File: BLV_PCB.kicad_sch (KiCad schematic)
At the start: 8 parts, among them J1 Cube0 JST-PH, J2 Cube0 JST-PH, J3 Cube0 JST-PH, J4 Micro_SD_Card

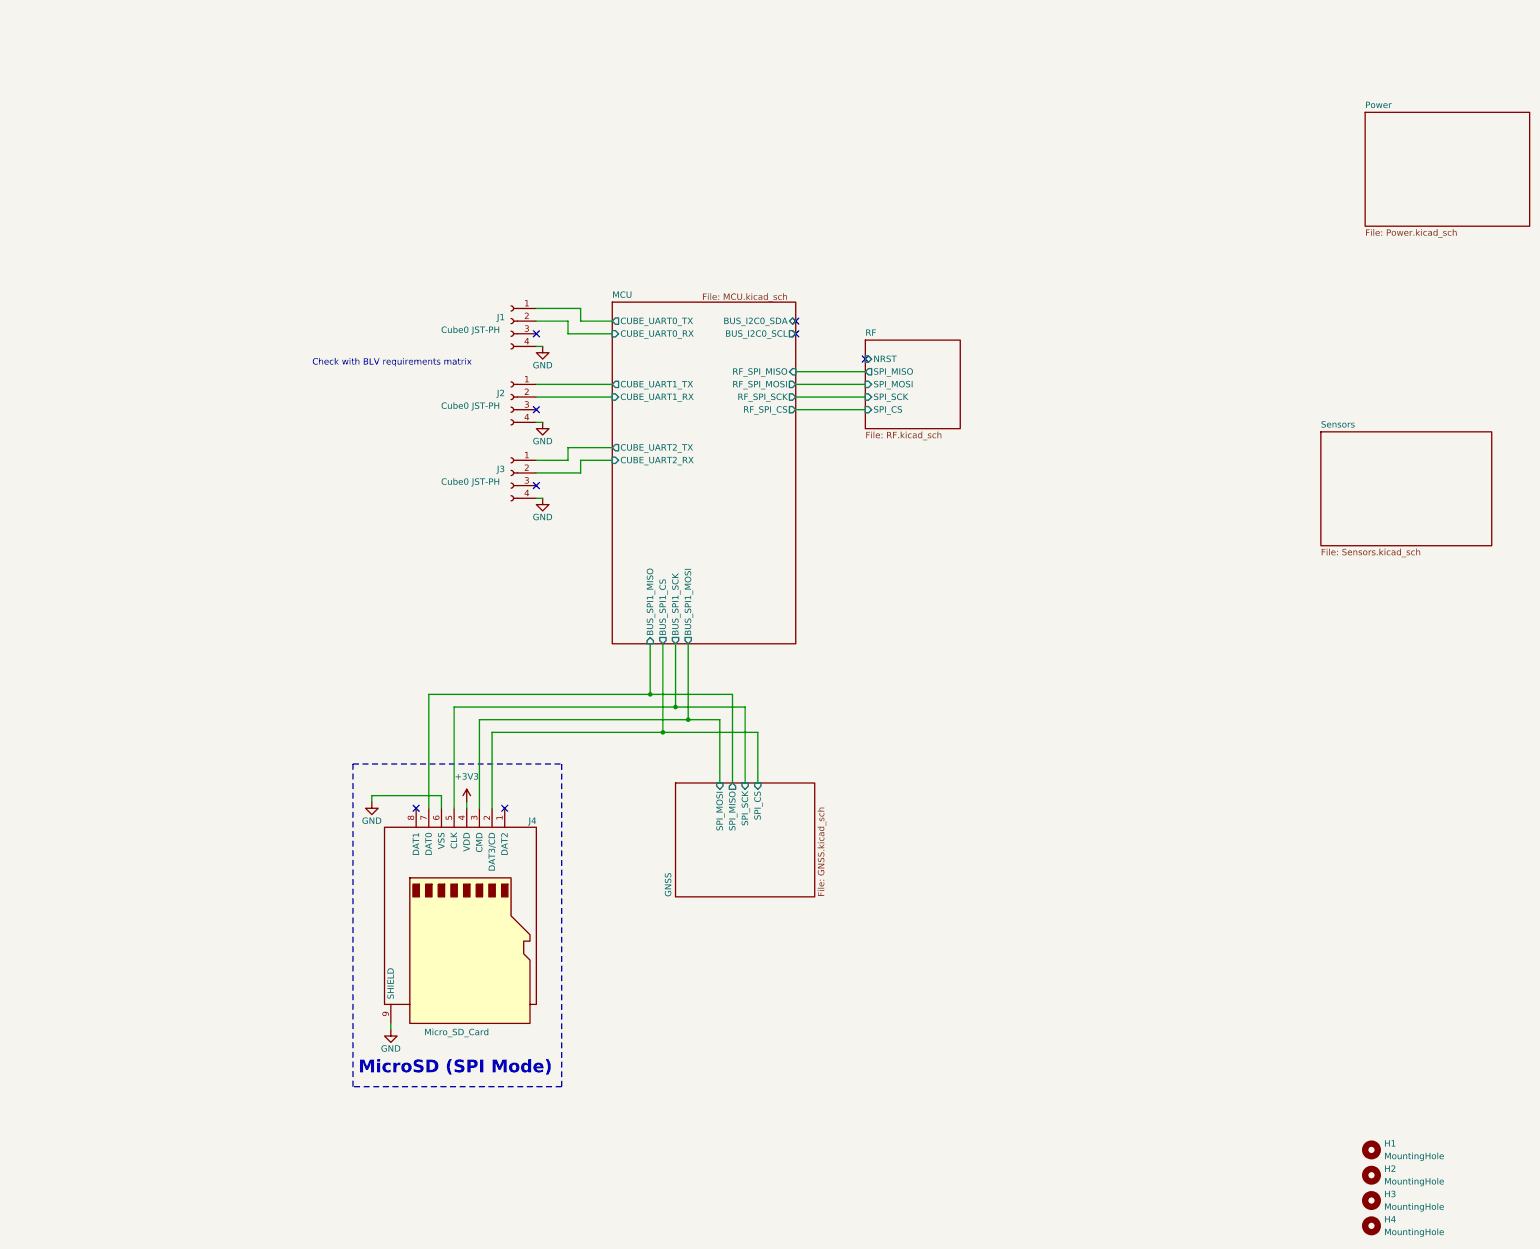
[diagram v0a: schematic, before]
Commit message: Added footprints & routing 30%
- Added Dupont debug headers for UARTs.
- Added footprints: 18650 battery, E32-400M30S.
- Remove Battery Charger due to reliability issue.
- Routing 5V SMPS, 3V3 Regulator, Battery Holder.
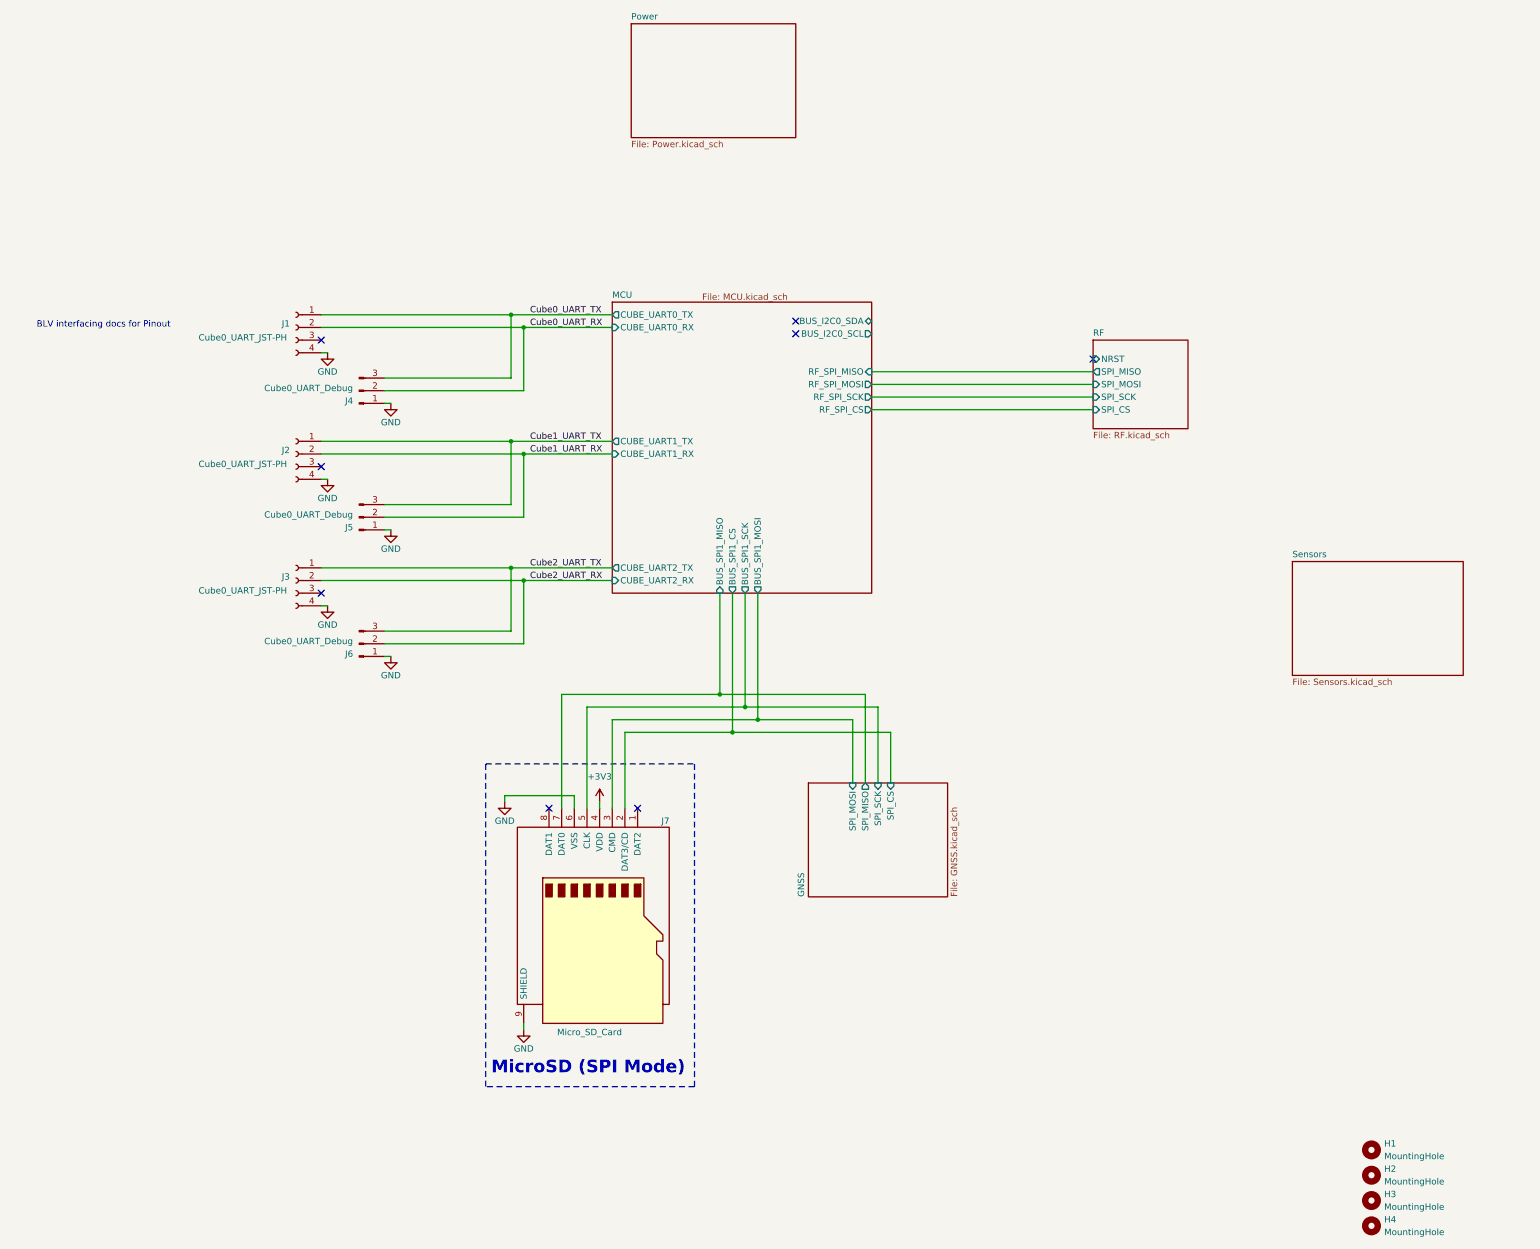
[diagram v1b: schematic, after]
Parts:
- added J4, J5, J6: Cube0_UART_Debug, Connector_PinHeader_2.54mm:PinHeader_1x03_P2.54mm_Vertical, symbol Connector:Conn_01x03_Pin
- J1, J2, J3: value Cube0 JST-PH -> Cube0_UART_JST-PH
- renumbered J4 to J7
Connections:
- net GND: now also J4.1 (Pin_1), J5.1 (Pin_1), J6.1 (Pin_1)
- net MCU/CUBE_UART0_RX renamed Cube0_UART_RX
- net Cube0_UART_RX: now also J4.2 (Pin_2)
- net MCU/CUBE_UART0_TX renamed Cube0_UART_TX
- net Cube0_UART_TX: now also J4.3 (Pin_3)
- net MCU/CUBE_UART1_RX renamed Cube1_UART_RX
- net Cube1_UART_RX: now also J5.2 (Pin_2)
- net MCU/CUBE_UART1_TX renamed Cube1_UART_TX
- net Cube1_UART_TX: now also J5.3 (Pin_3)
- net MCU/CUBE_UART2_RX renamed Cube2_UART_RX
- net Cube2_UART_RX: now also J6.2 (Pin_2)
- net MCU/CUBE_UART2_TX renamed Cube2_UART_TX
- net Cube2_UART_TX: now also J6.3 (Pin_3)
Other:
- note added: "BLV interfacing docs for Pinout"
- note removed: "Check with BLV requirements matrix"
- moved on the sheet: J1, J7

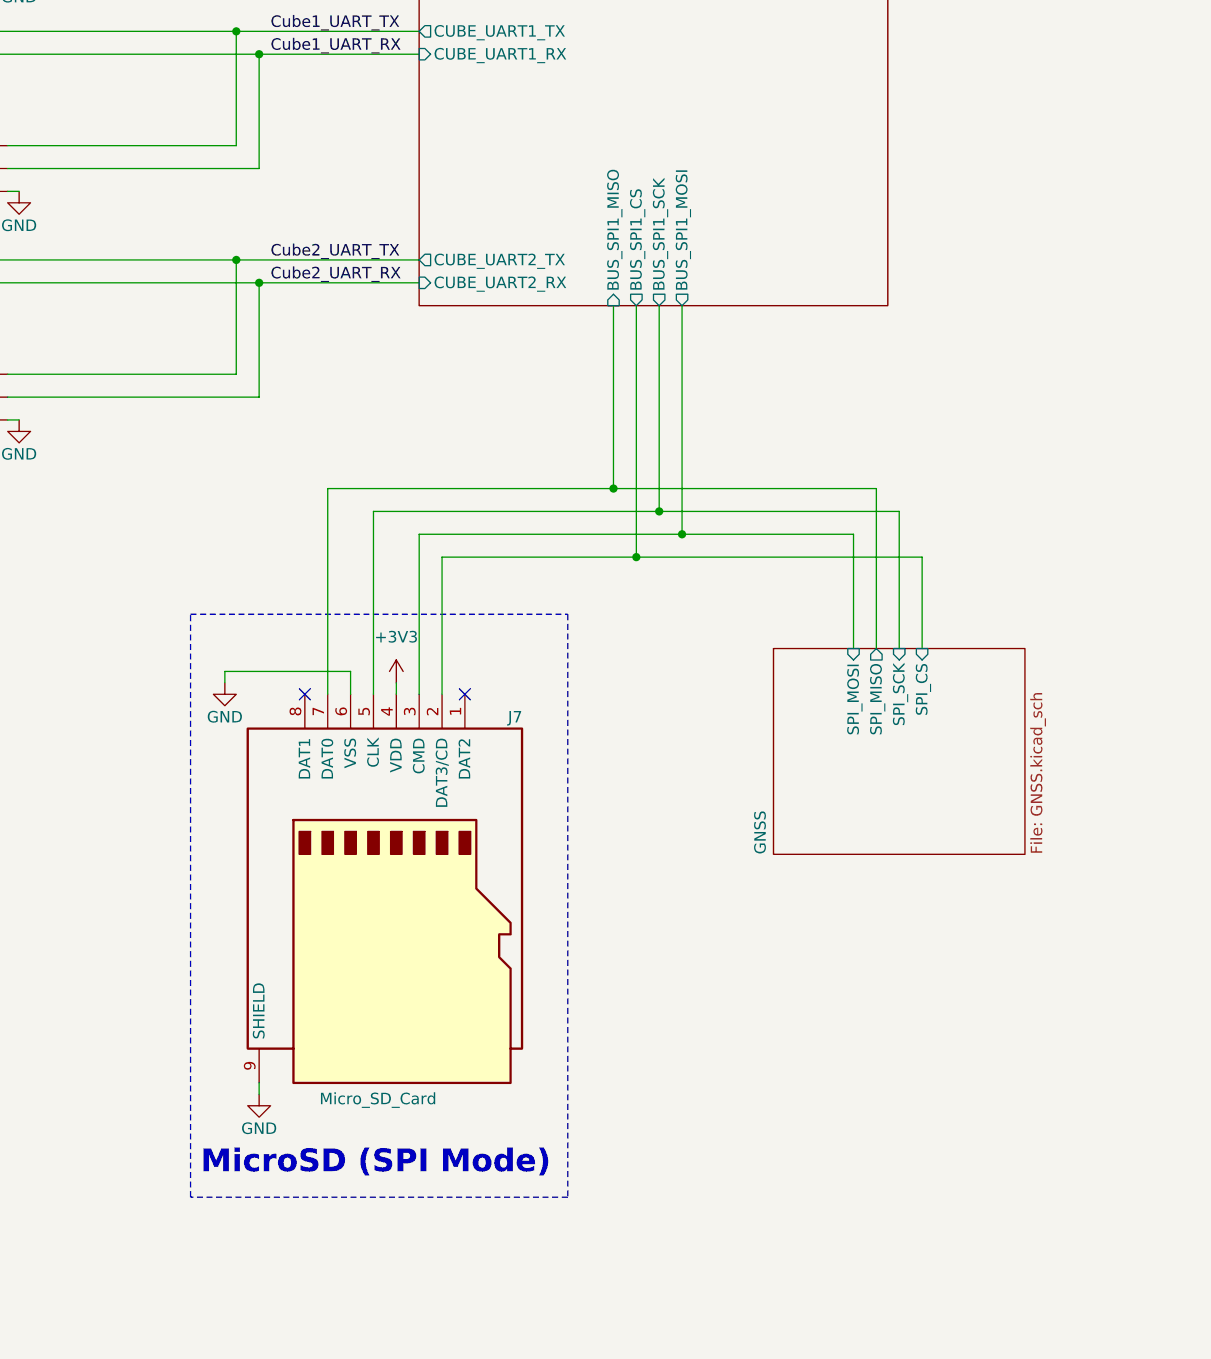
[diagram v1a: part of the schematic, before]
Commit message: Finished layout & DRC
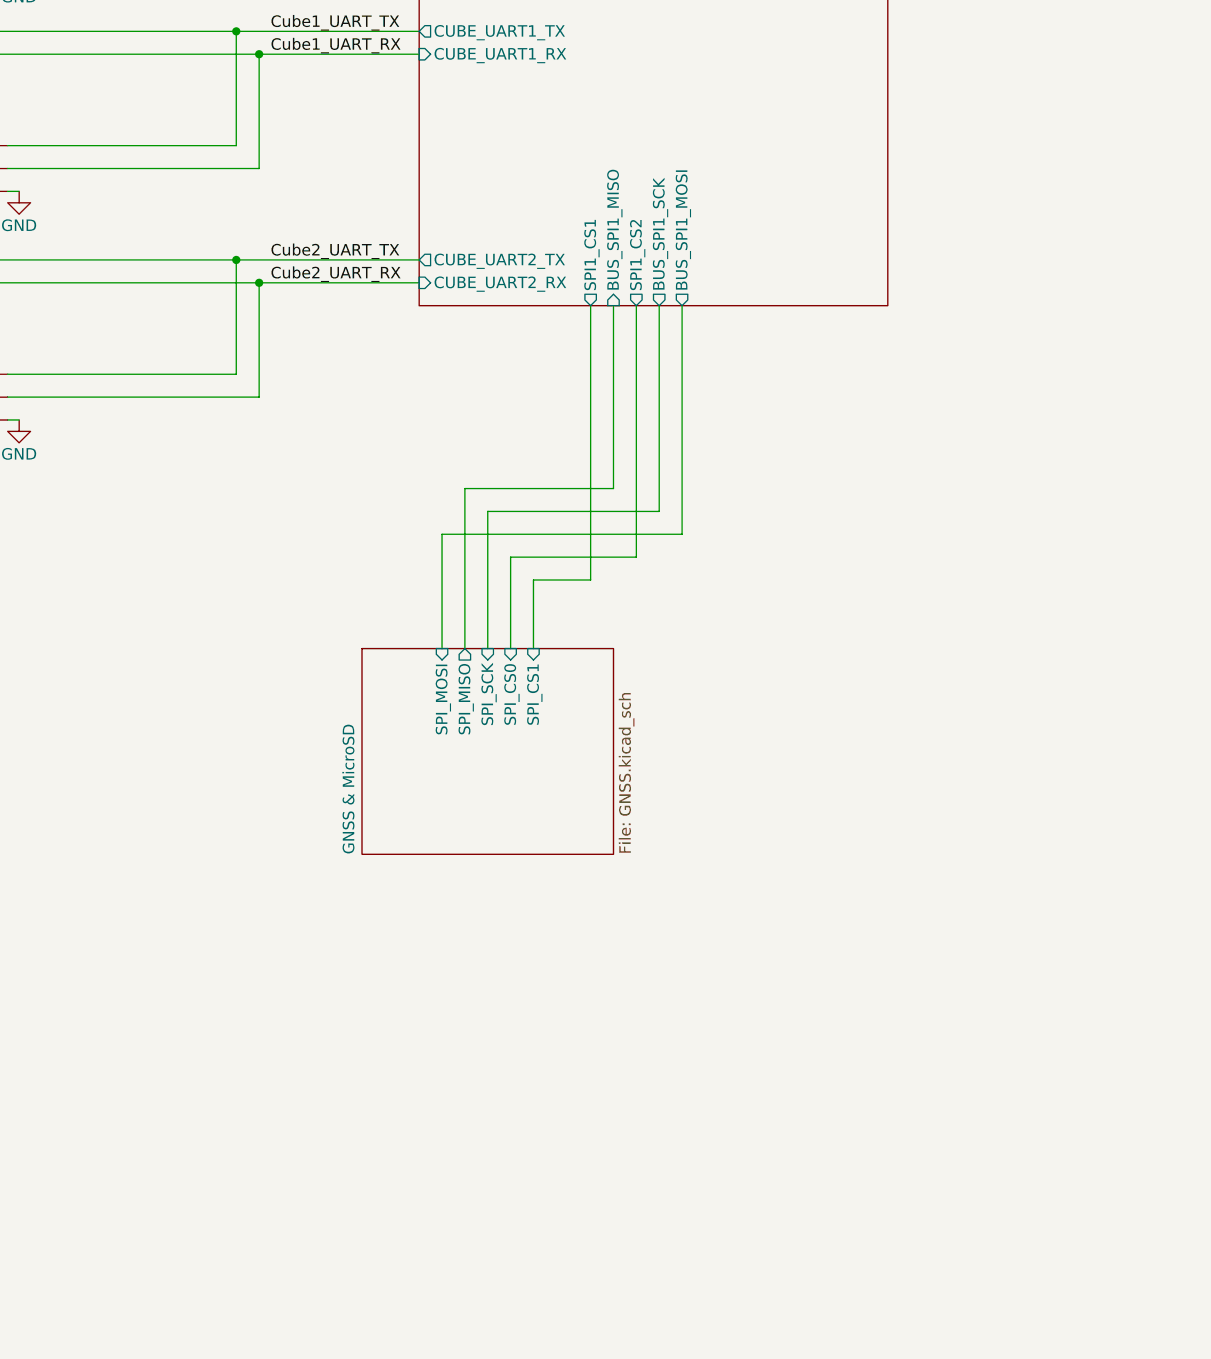
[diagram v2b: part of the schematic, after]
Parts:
- removed J7: Micro_SD_Card, Connector_Card:microSD_HC_Wuerth_693072010801, symbol Connector:Micro_SD_Card
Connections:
- no-connect marks 8 -> 6
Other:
- sheet GNSS renamed GNSS & MicroSD
- sheet GNSS & MicroSD ports: added SPI_CS0, SPI_CS1; removed SPI_CS
- sheet MCU ports: added SPI1_CS1, SPI1_CS2; removed BUS_SPI1_CS
- note removed: "MicroSD (SPI Mode)"
